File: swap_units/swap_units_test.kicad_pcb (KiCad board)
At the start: 2 copper layers, 9 parts, among them U1 LM324, U2 PIC18F452-IP

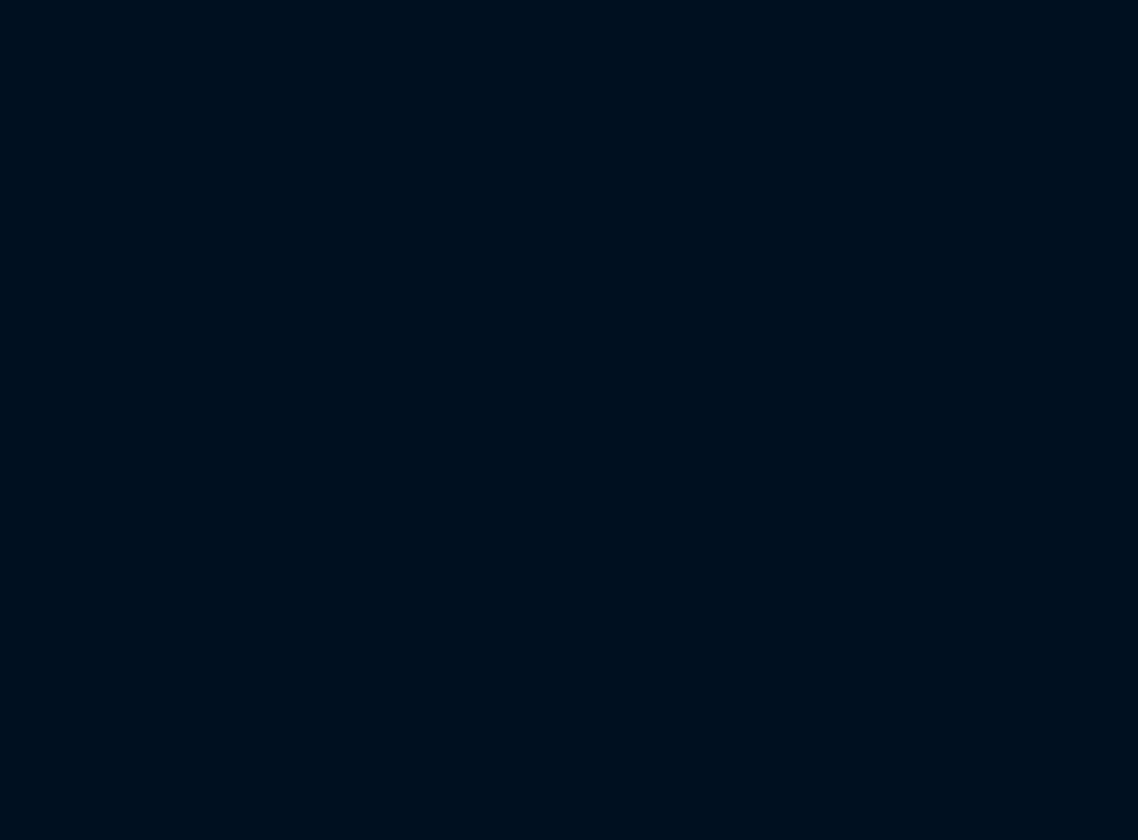
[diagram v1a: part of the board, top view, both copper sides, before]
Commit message: Updated test project to include multiple hierarchy
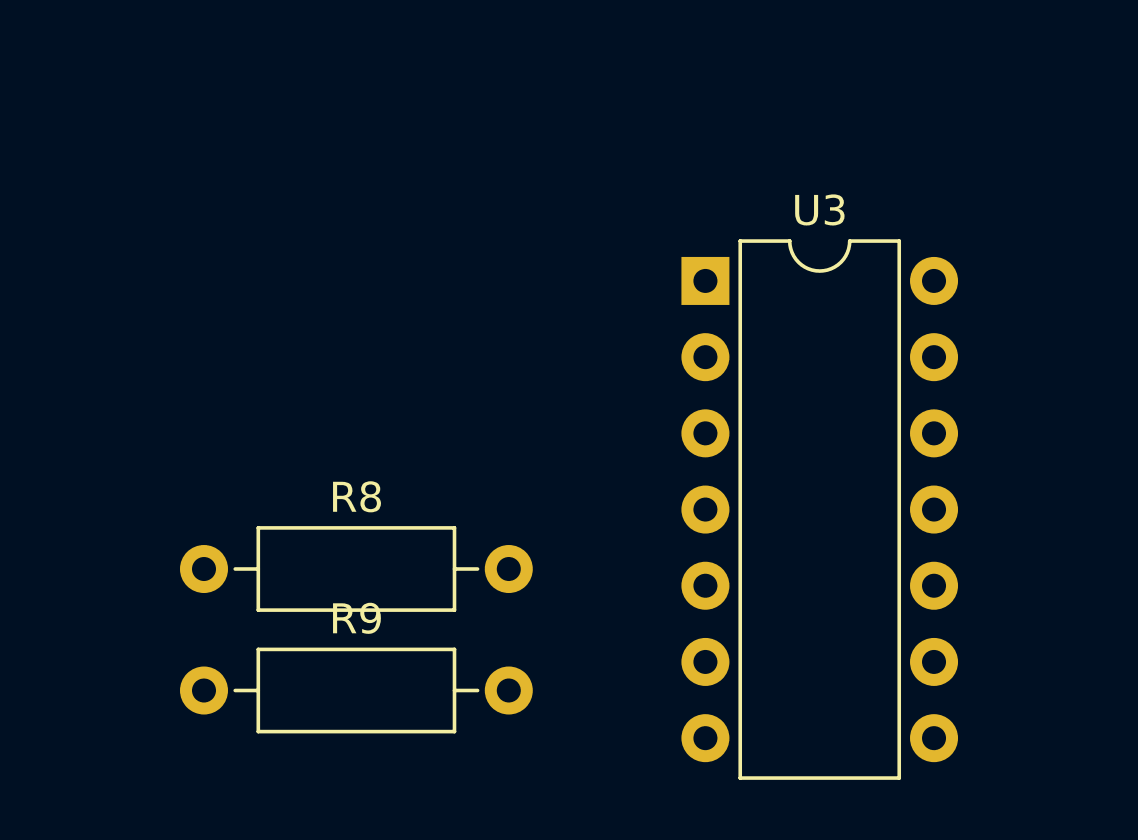
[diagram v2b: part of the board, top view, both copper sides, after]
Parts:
- added R8: R, Resistor_THT:R_Axial_DIN0207_L6.3mm_D2.5mm_P10.16mm_Horizontal, F.Cu at (97.2, 105.2)
- added R9: R, Resistor_THT:R_Axial_DIN0207_L6.3mm_D2.5mm_P10.16mm_Horizontal, F.Cu at (97.2, 109.2)
- added U3: LM324, Package_DIP:DIP-14_W7.62mm, F.Cu at (113.9, 95.6)
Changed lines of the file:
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@@
-(kicad_pcb (version 20171130) (host pcbnew "(5.1.0-rc2-4-g73f0b3087)")
+(kicad_pcb (version 20171130) (host pcbnew "(5.1.0)-1")
   (general
     (thickness 1.6)
@@
     (tracks 0)
     (zones 0)
-    (modules 9)
-    (nets 43)
+    (modules 12)
+    (nets 48)
   )
   (page A4)
@@
   (net 41 "Net-(U2-Pad20)")
   (net 42 "Net-(U2-Pad40)")
+  (net 43 "Net-(R8-Pad2)")
+  (net 44 /Level1/Level2b/out_level_2)
+  (net 45 "Net-(U3-Pad3)")
+  (net 46 "Net-(U3-Pad2)")
+  (net 47 "Net-(U3-Pad1)")
   (net_class Default "This is the default net class."
     (clearance 0.2)
@@
     (uvia_drill 0.1)
     (add_net +5V)
+    (add_net /Level1/Level2b/out_level_2)
     (add_net /Level1/out_level_1)
     (add_net /Level1/out_level_2)
@@
     (add_net "Net-(R4-Pad2)")
     (add_net "Net-(R6-Pad2)")
+    (add_net "Net-(R8-Pad2)")
     (add_net "Net-(U1-Pad1)")
     (add_net "Net-(U1-Pad6)")
@@
     (add_net "Net-(U2-Pad8)")
     (add_net "Net-(U2-Pad9)")
+    (add_net "Net-(U3-Pad1)")
+    (add_net "Net-(U3-Pad2)")
+    (add_net "Net-(U3-Pad3)")
+  )
+  (module Package_DIP:DIP-14_W7.62mm (layer F.Cu)
+    (at 113.901001 95.555001)
+    (descr "14-lead though-hole mounted DIP package, row spacing 7.62 mm (300 mils)")
+    (tags "THT DIP DIL PDIP 2.54mm 7.62mm 300mil")
+    (fp_text reference U3 (at 3.81 -2.33) (layer F.SilkS)
+      (effects (font (size 1 1) (thickness 0.15)))
+    )
+    (fp_text value LM324 (at 3.81 17.57) (layer F.Fab)
+      (effects (font (size 1 1) (thickness 0.15)))
+    )
+    (fp_text user %R (at 3.81 7.62) (layer F.Fab)
+      (effects (font (size 1 1) (thickness 0.15)))
+    )
+    (fp_line (start 8.7 -1.55) (end -1.1 -1.55) (layer F.CrtYd) (width 0.05))
+    (fp_line (start 8.7 16.8) (end 8.7 -1.55) (layer F.CrtYd) (width 0.05))
+    (fp_line (start -1.1 16.8) (end 8.7 16.8) (layer F.CrtYd) (width 0.05))
+    (fp_line (start -1.1 -1.55) (end -1.1 16.8) (layer F.CrtYd) (width 0.05))
+    (fp_line (start 6.46 -1.33) (end 4.81 -1.33) (layer F.SilkS) (width 0.12))
+    (fp_line (start 6.46 16.57) (end 6.46 -1.33) (layer F.SilkS) (width 0.12))
+    (fp_line (start 1.16 16.57) (end 6.46 16.57) (layer F.SilkS) (width 0.12))
+    (fp_line (start 1.16 -1.33) (end 1.16 16.57) (layer F.SilkS) (width 0.12))
+    (fp_line (start 2.81 -1.33) (end 1.16 -1.33) (layer F.SilkS) (width 0.12))
+    (fp_line (start 0.635 -0.27) (end 1.635 -1.27) (layer F.Fab) (width 0.1))
+    (fp_line (start 0.635 16.51) (end 0.635 -0.27) (layer F.Fab) (width 0.1))
+    (fp_line (start 6.985 16.51) (end 0.635 16.51) (layer F.Fab) (width 0.1))
+    (fp_line (start 6.985 -1.27) (end 6.985 16.51) (layer F.Fab) (width 0.1))
+    (fp_line (start 1.635 -1.27) (end 6.985 -1.27) (layer F.Fab) (width 0.1))
+    (fp_arc (start 3.81 -1.33) (end 2.81 -1.33) (angle -180) (layer F.SilkS) (width 0.12))
+    (pad 14 thru_hole oval (at 7.62 0) (size 1.6 1.6) (drill 0.8) (layers *.Cu *.Mask)
+      (net 44 /Level1/Level2b/out_level_2))
+    (pad 7 thru_hole oval (at 0 15.24) (size 1.6 1.6) (drill 0.8) (layers *.Cu *.Mask))
+    (pad 13 thru_hole oval (at 7.62 2.54) (size 1.6 1.6) (drill 0.8) (layers *.Cu *.Mask)
+      (net 44 /Level1/Level2b/out_level_2))
+    (pad 6 thru_hole oval (at 0 12.7) (size 1.6 1.6) (drill 0.8) (layers *.Cu *.Mask))
+    (pad 12 thru_hole oval (at 7.62 5.08) (size 1.6 1.6) (drill 0.8) (layers *.Cu *.Mask)
+      (net 43 "Net-(R8-Pad2)"))
+    (pad 5 thru_hole oval (at 0 10.16) (size 1.6 1.6) (drill 0.8) (layers *.Cu *.Mask))
+    (pad 11 thru_hole oval (at 7.62 7.62) (size 1.6 1.6) (drill 0.8) (layers *.Cu *.Mask))
+    (pad 4 thru_hole oval (at 0 7.62) (size 1.6 1.6) (drill 0.8) (layers *.Cu *.Mask))
+    (pad 10 thru_hole oval (at 7.62 10.16) (size 1.6 1.6) (drill 0.8) (layers *.Cu *.Mask))
+    (pad 3 thru_hole oval (at 0 5.08) (size 1.6 1.6) (drill 0.8) (layers *.Cu *.Mask)
+      (net 45 "Net-(U3-Pad3)"))
+    (pad 9 thru_hole oval (at 7.62 12.7) (size 1.6 1.6) (drill 0.8) (layers *.Cu *.Mask))
+    (pad 2 thru_hole oval (at 0 2.54) (size 1.6 1.6) (drill 0.8) (layers *.Cu *.Mask)
+      (net 46 "Net-(U3-Pad2)"))
+    (pad 8 thru_hole oval (at 7.62 15.24) (size 1.6 1.6) (drill 0.8) (layers *.Cu *.Mask))
+    (pad 1 thru_hole rect (at 0 0) (size 1.6 1.6) (drill 0.8) (layers *.Cu *.Mask)
+      (net 47 "Net-(U3-Pad1)"))
+    (model ${KISYS3DMOD}/Package_DIP.3dshapes/DIP-14_W7.62mm.wrl
+      (at (xyz 0 0 0))
+      (scale (xyz 1 1 1))
+      (rotate (xyz 0 0 0))
+    )
   )
   (module Resistor_THT:R_Axial_DIN0207_L6.3mm_D2.5mm_P10.16mm_Horizontal (layer F.Cu)
+    (at 97.187001 109.207001)
+    (descr "Resistor, Axial_DIN0207 series, Axial, Horizontal, pin pitch=10.16mm, 0.25W = 1/4W, length*diameter=6.3*2.5mm^2, http://cdn-reichelt.de/documents/datenblatt/B400/1_4W%23YAG.pdf")
+    (tags "Resistor Axial_DIN0207 series Axial Horizontal pin pitch 10.16mm 0.25W = 1/4W length 6.3mm diameter 2.5mm")
+    (fp_text reference R9 (at 5.08 -2.37) (layer F.SilkS)
+      (effects (font (size 1 1) (thickness 0.15)))
+    )
+    (fp_text value R (at 5.08 2.37) (layer F.Fab)
+      (effects (font (size 1 1) (thickness 0.15)))
+    )
+    (fp_text user %R (at 5.08 0) (layer F.Fab)
+      (effects (font (size 1 1) (thickness 0.15)))
+    )
+    (fp_line (start 11.21 -1.5) (end -1.05 -1.5) (layer F.CrtYd) (width 0.05))
+    (fp_line (start 11.21 1.5) (end 11.21 -1.5) (layer F.CrtYd) (width 0.05))
+    (fp_line (start -1.05 1.5) (end 11.21 1.5) (layer F.CrtYd) (width 0.05))
+    (fp_line (start -1.05 -1.5) (end -1.05 1.5) (layer F.CrtYd) (width 0.05))
+    (fp_line (start 9.12 0) (end 8.35 0) (layer F.SilkS) (width 0.12))
+    (fp_line (start 1.04 0) (end 1.81 0) (layer F.SilkS) (width 0.12))
+    (fp_line (start 8.35 -1.37) (end 1.81 -1.37) (layer F.SilkS) (width 0.12))
+    (fp_line (start 8.35 1.37) (end 8.35 -1.37) (layer F.SilkS) (width 0.12))
+    (fp_line (start 1.81 1.37) (end 8.35 1.37) (layer F.SilkS) (width 0.12))
+    (fp_line (start 1.81 -1.37) (end 1.81 1.37) (layer F.SilkS) (width 0.12))
+    (fp_line (start 10.16 0) (end 8.23 0) (layer F.Fab) (width 0.1))
+    (fp_line (start 0 0) (end 1.93 0) (layer F.Fab) (width 0.1))
+    (fp_line (start 8.23 -1.25) (end 1.93 -1.25) (layer F.Fab) (width 0.1))
+    (fp_line (start 8.23 1.25) (end 8.23 -1.25) (layer F.Fab) (width 0.1))
+    (fp_line (start 1.93 1.25) (end 8.23 1.25) (layer F.Fab) (width 0.1))
+    (fp_line (start 1.93 -1.25) (end 1.93 1.25) (layer F.Fab) (width 0.1))
+    (pad 2 thru_hole oval (at 10.16 0) (size 1.6 1.6) (drill 0.8) (layers *.Cu *.Mask)
+      (net 4 GND))
+    (pad 1 thru_hole circle (at 0 0) (size 1.6 1.6) (drill 0.8) (layers *.Cu *.Mask)
+      (net 43 "Net-(R8-Pad2)"))
+    (model ${KISYS3DMOD}/Resistor_THT.3dshapes/R_Axial_DIN0207_L6.3mm_D2.5mm_P10.16mm_Horizontal.wrl
+      (at (xyz 0 0 0))
+      (scale (xyz 1 1 1))
+      (rotate (xyz 0 0 0))
+    )
+  )
+  (module Resistor_THT:R_Axial_DIN0207_L6.3mm_D2.5mm_P10.16mm_Horizontal (layer F.Cu)
+    (at 97.187001 105.157001)
+    (descr "Resistor, Axial_DIN0207 series, Axial, Horizontal, pin pitch=10.16mm, 0.25W = 1/4W, length*diameter=6.3*2.5mm^2, http://cdn-reichelt.de/documents/datenblatt/B400/1_4W%23YAG.pdf")
+    (tags "Resistor Axial_DIN0207 series Axial Horizontal pin pitch 10.16mm 0.25W = 1/4W length 6.3mm diameter 2.5mm")
+    (fp_text reference R8 (at 5.08 -2.37) (layer F.SilkS)
+      (effects (font (size 1 1) (thickness 0.15)))
+    )
+    (fp_text value R (at 5.08 2.37) (layer F.Fab)
+      (effects (font (size 1 1) (thickness 0.15)))
+    )
+    (fp_text user %R (at 5.08 0) (layer F.Fab)
+      (effects (font (size 1 1) (thickness 0.15)))
+    )
+    (fp_line (start 11.21 -1.5) (end -1.05 -1.5) (layer F.CrtYd) (width 0.05))
+    (fp_line (start 11.21 1.5) (end 11.21 -1.5) (layer F.CrtYd) (width 0.05))
+    (fp_line (start -1.05 1.5) (end 11.21 1.5) (layer F.CrtYd) (width 0.05))
+    (fp_line (start -1.05 -1.5) (end -1.05 1.5) (layer F.CrtYd) (width 0.05))
+    (fp_line (start 9.12 0) (end 8.35 0) (layer F.SilkS) (width 0.12))
+    (fp_line (start 1.04 0) (end 1.81 0) (layer F.SilkS) (width 0.12))
+    (fp_line (start 8.35 -1.37) (end 1.81 -1.37) (layer F.SilkS) (width 0.12))
+    (fp_line (start 8.35 1.37) (end 8.35 -1.37) (layer F.SilkS) (width 0.12))
+    (fp_line (start 1.81 1.37) (end 8.35 1.37) (layer F.SilkS) (width 0.12))
+    (fp_line (start 1.81 -1.37) (end 1.81 1.37) (layer F.SilkS) (width 0.12))
+    (fp_line (start 10.16 0) (end 8.23 0) (layer F.Fab) (width 0.1))
+    (fp_line (start 0 0) (end 1.93 0) (layer F.Fab) (width 0.1))
+    (fp_line (start 8.23 -1.25) (end 1.93 -1.25) (layer F.Fab) (width 0.1))
+    (fp_line (start 8.23 1.25) (end 8.23 -1.25) (layer F.Fab) (width 0.1))
+    (fp_line (start 1.93 1.25) (end 8.23 1.25) (layer F.Fab) (width 0.1))
+    (fp_line (start 1.93 -1.25) (end 1.93 1.25) (layer F.Fab) (width 0.1))
+    (pad 2 thru_hole oval (at 10.16 0) (size 1.6 1.6) (drill 0.8) (layers *.Cu *.Mask)
+      (net 43 "Net-(R8-Pad2)"))
+    (pad 1 thru_hole circle (at 0 0) (size 1.6 1.6) (drill 0.8) (layers *.Cu *.Mask)
+      (net 1 +5V))
+    (model ${KISYS3DMOD}/Resistor_THT.3dshapes/R_Axial_DIN0207_L6.3mm_D2.5mm_P10.16mm_Horizontal.wrl
+      (at (xyz 0 0 0))
+      (scale (xyz 1 1 1))
+      (rotate (xyz 0 0 0))
+    )
+  )
+  (module Resistor_THT:R_Axial_DIN0207_L6.3mm_D2.5mm_P10.16mm_Horizontal (layer F.Cu)
